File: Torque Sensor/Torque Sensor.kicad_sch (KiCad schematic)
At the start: 9 parts, among them U2 MCP3561R, U4 AP2112K-3.3 (REG LINEAR 3.3V)

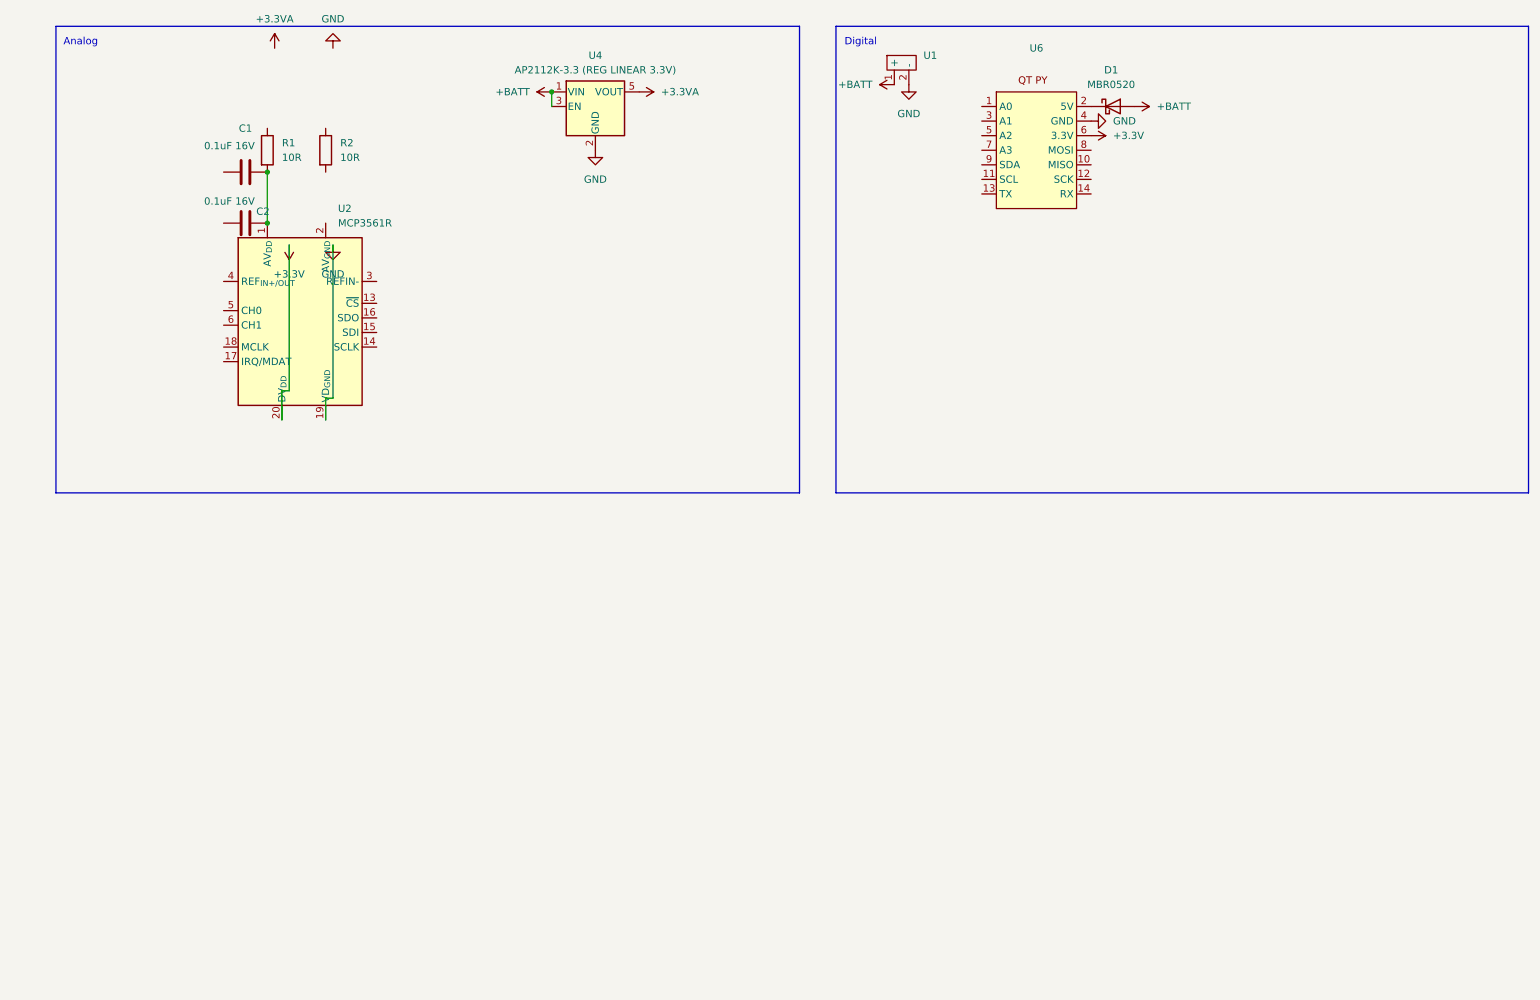
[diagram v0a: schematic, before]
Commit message: Reverted to older schematic
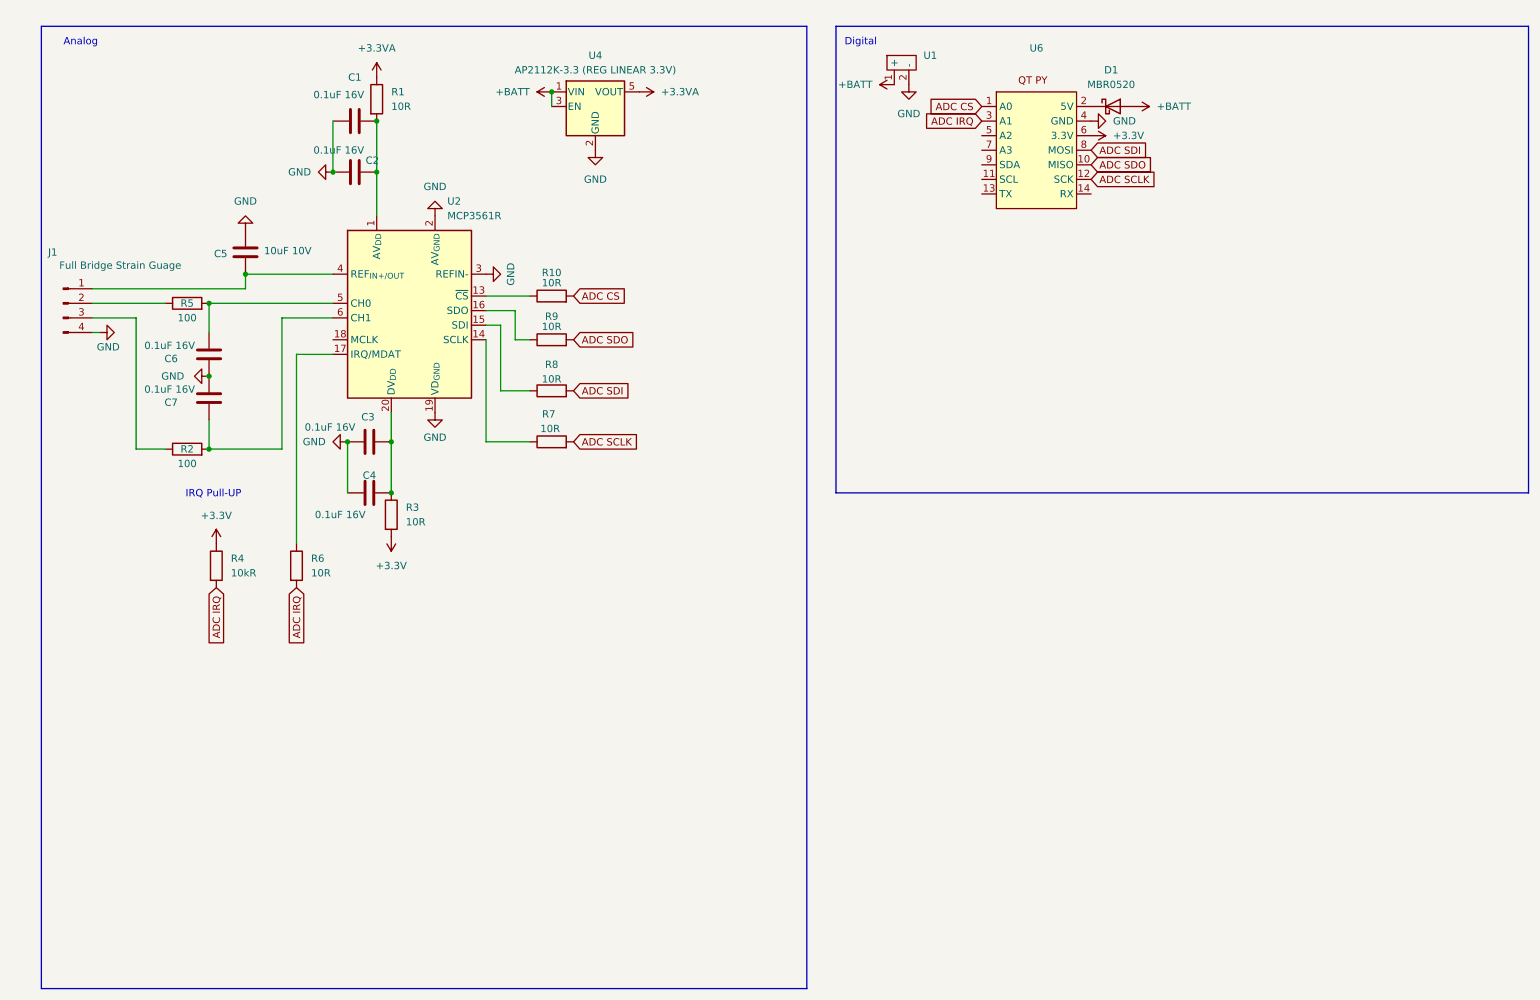
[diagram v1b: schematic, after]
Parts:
- added C3, C4, C6, C7: 0.1uF 16V, symbol Device:C
- added C5: 10uF 10V, symbol Device:C
- added J1: Full Bridge Strain Guage, symbol Connector:Conn_01x04_Pin
- added R10, R3, R6, R7, R8, R9: 10R, symbol Device:R
- added R4: 10kR, symbol Device:R
- added R5: 100, symbol Device:R
- R2: value 10R -> 100
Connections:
- net +3.3V: now also R3.2, R4.1; no longer U2.20 (DV_{DD})
- net +3.3VA: now also R1.1
- net GND: now also C1.1, C2.1, U2.2 (AV_{GND}), U2.3 (REFIN-), C3.1, C4.1, C5.2, C6.1, C7.2, J1.4 (Pin_4)
- net ADC CS: now reaches U6.1 (A0)
- net ADC CS: now also R10.2
- net ADC SDO: now reaches U6.10 (MISO)
- net ADC SDO: now also R9.2
- net ADC SCLK: now reaches U6.12 (SCK)
- net ADC SCLK: now also R7.2
- net ADC IRQ: now reaches U6.3 (A1)
- net ADC IRQ: now also R4.2, R6.2
- net ADC SDI: now reaches U6.8 (MOSI)
- net ADC SDI: now also R8.2
- net at U2.13 (~{CS}): now also R10.1
- net at U2.14 (SCLK): now also R7.1
- net at U2.15 (SDI): now also R8.1
- net at U2.16 (SDO): now also R9.1
- net at U2.17 (IRQ/MDAT): now also R6.1
- net at U2.4 (REF_{IN+/OUT}): now also C5.1, J1.1 (Pin_1)
- net at U2.5 (CH0): now also C6.2, R5.2
- net at U2.6 (CH1): now also R2.2, C7.1
- net at R2.1: now also J1.3 (Pin_3)
- new net: J1.2 (Pin_2), R5.1
- new net: C3.2, C4.2, R3.1, U2.20 (DV_{DD})
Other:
- note added: "IRQ Pull-UP"
- moved on the sheet: C1, C2, R1, U2

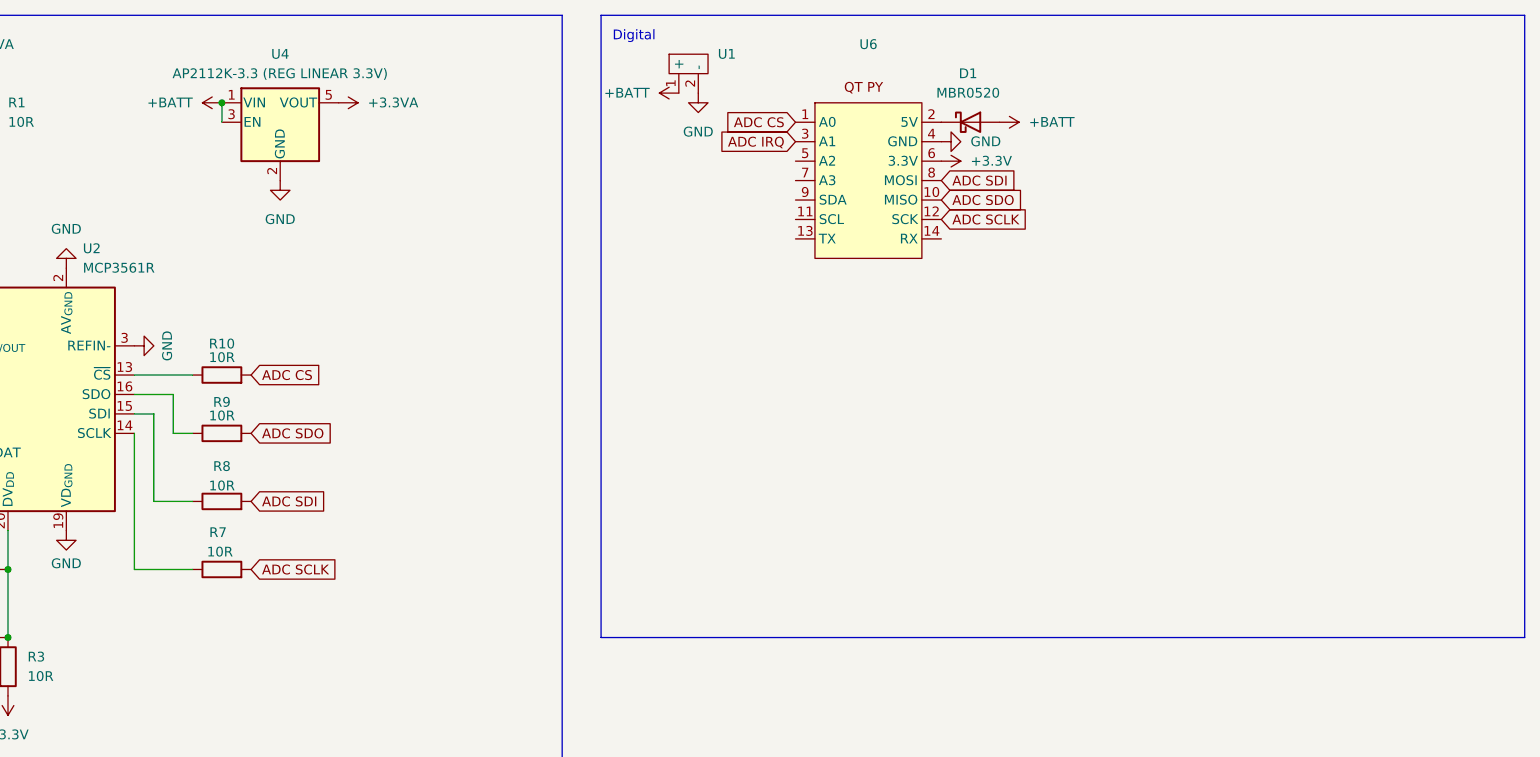
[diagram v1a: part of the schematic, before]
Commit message: Changed board to Feather rp2040 for charging circuitry, assigned footprints to caps and resistors.
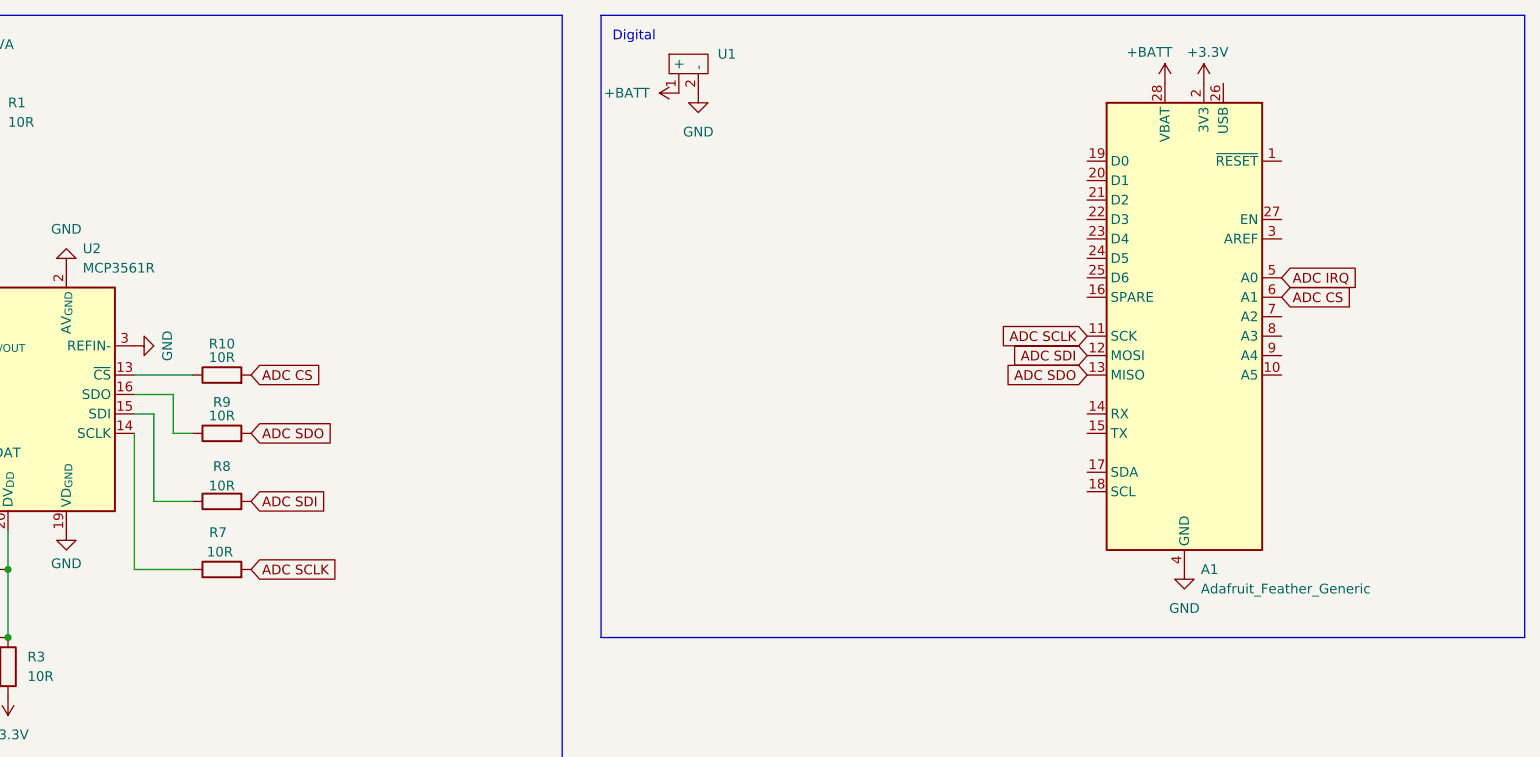
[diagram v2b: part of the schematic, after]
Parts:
- removed D1: MBR0520, Diode_SMD:D_SOD-123, symbol Diode:MBR0520
- removed U4: AP2112K-3.3 (REG LINEAR 3.3V), Package_TO_SOT_SMD:SOT-23-5, symbol Regulator_Linear:AP2112K-3.3
- removed U6: ~, TestLib:Adafruit QT PY, symbol New_Library:QT_PY
- added A1: Adafruit_Feather_Generic, Module:Adafruit_Feather, symbol MCU_Module:Adafruit_Feather_Generic
- C1, C2, C3, C4, C5, C6, C7: footprint (none) -> Capacitor_SMD:C_0805_2012Metric
- J1: footprint (none) -> Connector_PinHeader_1.00mm:PinHeader_1x04_P1.00mm_Vertical
- R1, R10, R2, R3, R4, R5, R6, R7, R8, R9: footprint (none) -> Resistor_SMD:R_0805_2012Metric
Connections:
- net +3.3V: now also A1.2 (3V3)
- net +BATT: now also A1.28 (VBAT)
- net ADC CS: now also A1.6 (A1)
- net ADC IRQ: now also A1.5 (A0)
- net ADC SCLK: now also A1.11 (SCK)
- net ADC SDI: now also A1.12 (MOSI)
- net ADC SDO: now also A1.13 (MISO)
- net GND: now also A1.4 (GND)

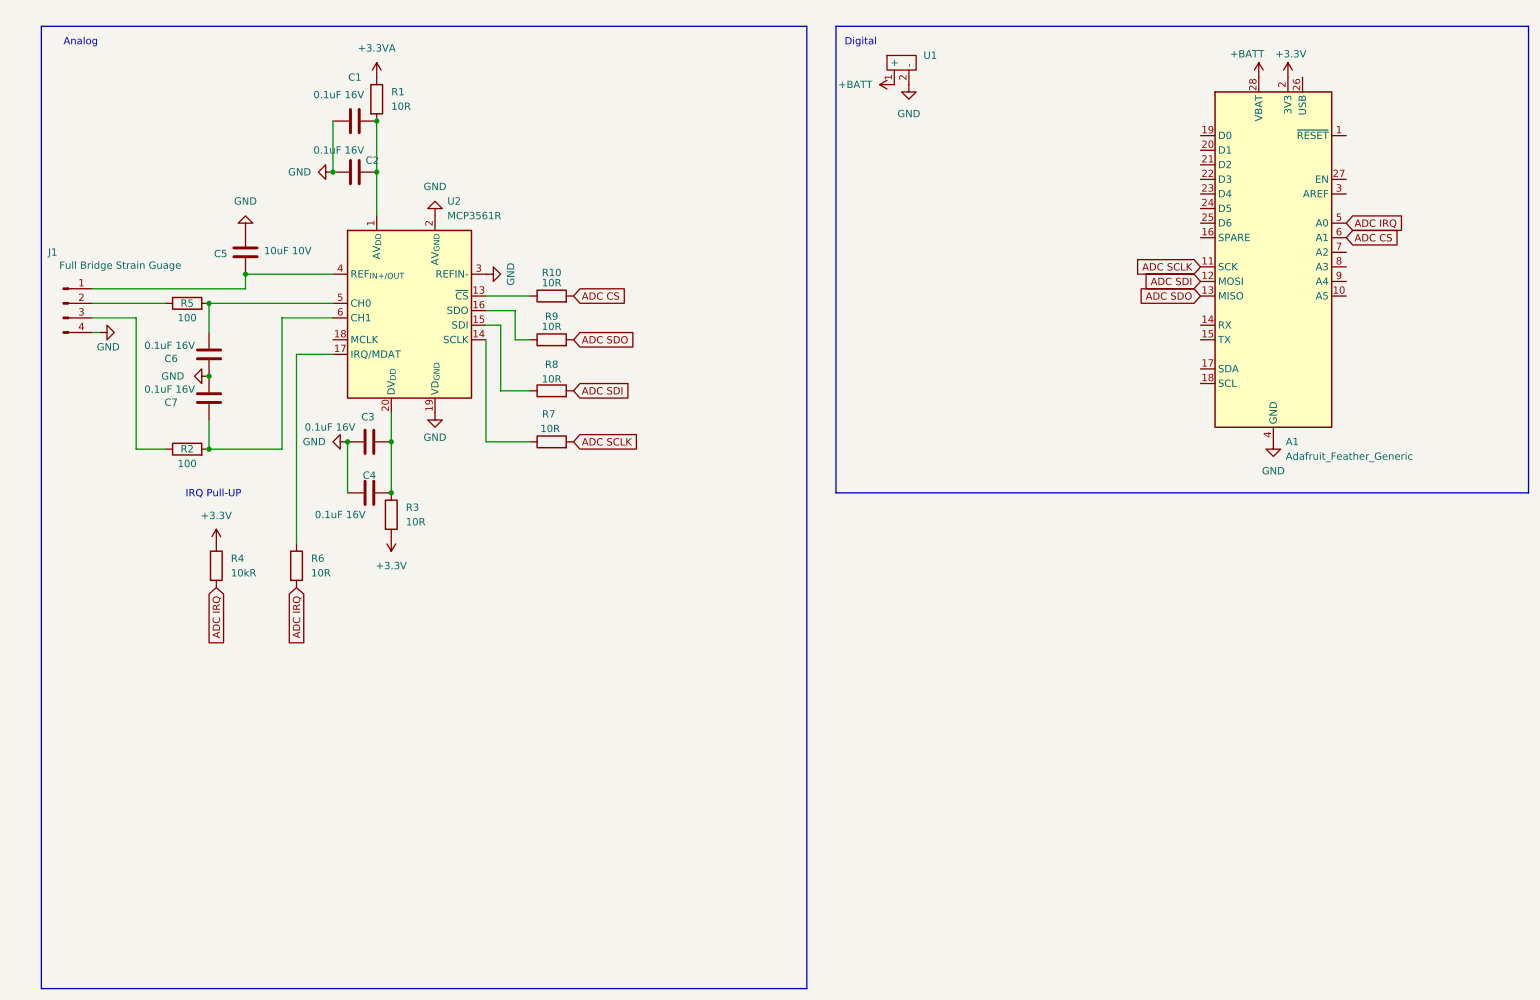
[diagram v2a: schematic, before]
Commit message: Changed ADC to the more JLC stocked AD7173-8 (Rev. B)
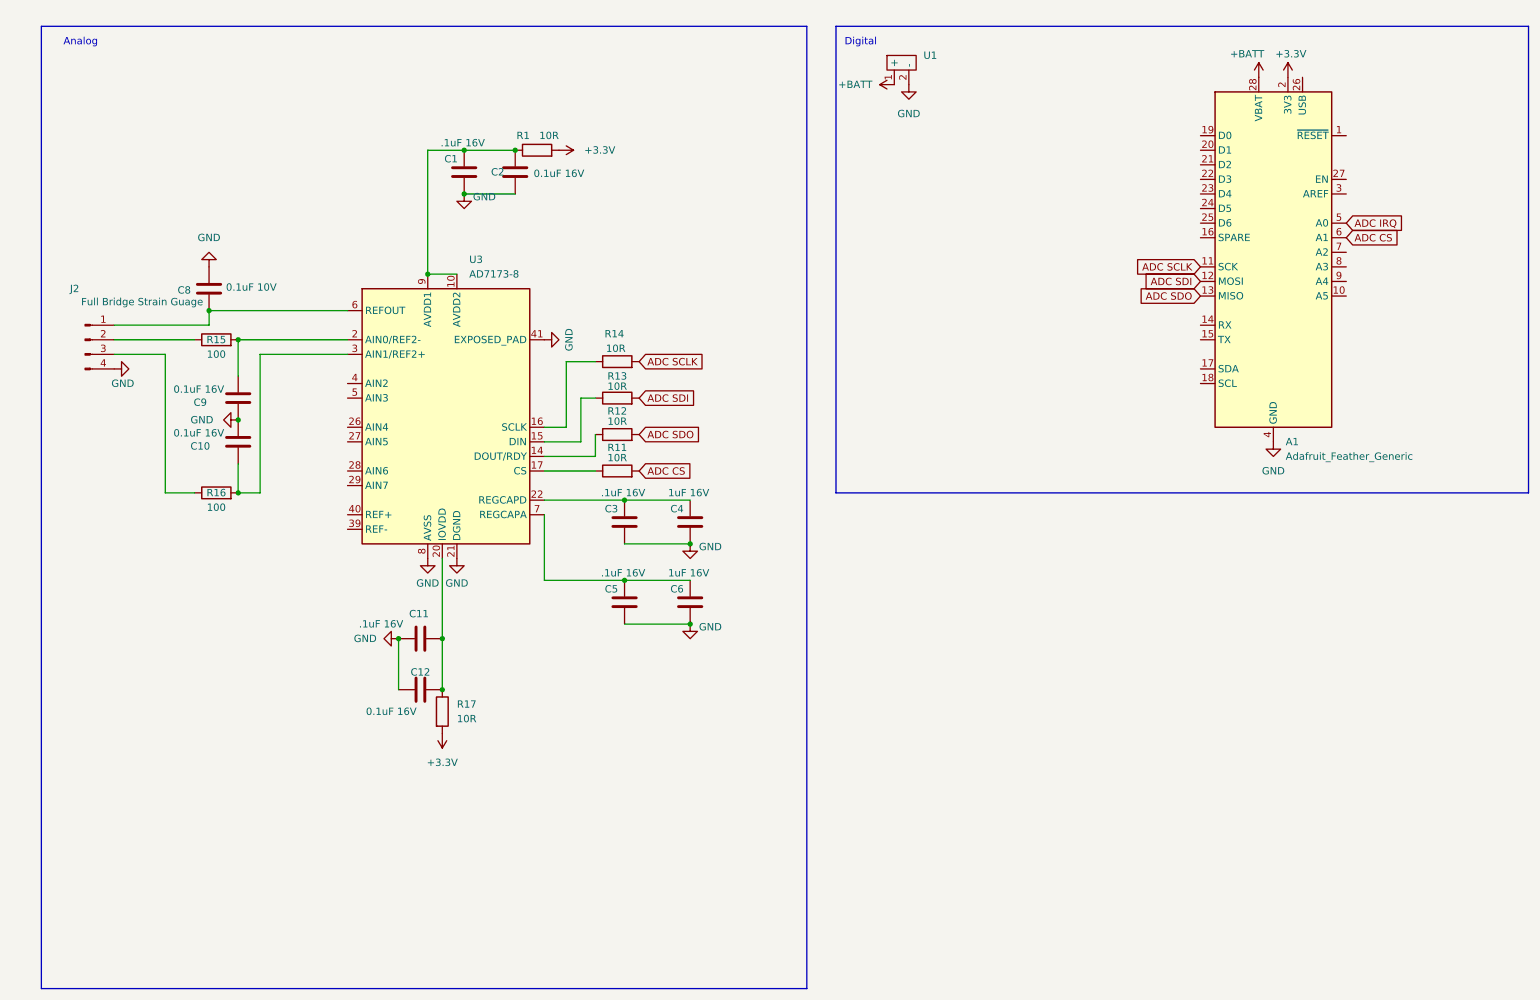
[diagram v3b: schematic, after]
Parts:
- removed C7: 0.1uF 16V, Capacitor_SMD:C_0805_2012Metric, symbol Device:C
- removed J1: Full Bridge Strain Guage, Connector_PinHeader_1.00mm:PinHeader_1x04_P1.00mm_Vertical, symbol Connector:Conn_01x04_Pin
- removed R10, R3, R6, R7, R8, R9: 10R, Resistor_SMD:R_0805_2012Metric, symbol Device:R
- removed R2, R5: 100, Resistor_SMD:R_0805_2012Metric, symbol Device:R
- removed R4: 10kR, Resistor_SMD:R_0805_2012Metric, symbol Device:R
- removed U2: MCP3561R, Package_SO:TSSOP-20_4.4x6.5mm_P0.65mm, symbol Analog_ADC:AD7327
- added C10, C12, C9: 0.1uF 16V, Capacitor_SMD:C_0805_2012Metric, symbol Device:C
- added C11: .1uF 16V, Capacitor_SMD:C_0805_2012Metric, symbol Device:C
- added C8: 0.1uF 10V, Capacitor_SMD:C_0805_2012Metric, symbol Device:C
- added J2: Full Bridge Strain Guage, Connector_PinHeader_1.00mm:PinHeader_1x04_P1.00mm_Vertical, symbol Connector:Conn_01x04_Pin
- added R11, R12, R13, R14, R17: 10R, Resistor_SMD:R_0805_2012Metric, symbol Device:R
- added R15, R16: 100, Resistor_SMD:R_0805_2012Metric, symbol Device:R
- added U3: AD7173-8, Package_CSP:LFCSP-40-1EP_6x6mm_P0.5mm_EP3.9x3.9mm, symbol New_Library:AD7173-8
- C1, C3: value 0.1uF 16V -> .1uF 16V
- C4, C6: value 0.1uF 16V -> 1uF 16V
- C5: value 10uF 10V -> .1uF 16V
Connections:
- net +3.3VA is gone; now on net AVDD: R1.1
- net +3.3V: now also R1.2, R17.2
- net ADC CS: now also R11.2
- net ADC SCLK: now also R14.2
- net ADC SDI: now also R13.2
- net ADC SDO: now also R12.2
- net GND: now also C5.1, C10.2, C11.1, C12.1, C8.2, C9.1, J2.4 (Pin_4), U3.21 (DGND), U3.22 (REGCAPD), U3.28 (AGND), U3.29 (AGND), U3.41 (EXPOSED_PAD), U3.5 (AGND), U3.8 (NC); no longer C5.2
- net AVDD: now reaches C1.2, C2.2
- net AVDD: now also U3.10 (AVDD2), U3.4 (AVDD), U3.40 (AVDD), U3.9 (AVDD1); no longer R1.2
- net at C3.2, C4.2: now also U3.22 (REGCAPD)
- net at C6.2: now also C5.2, U3.7 (REGCAPA)
- new net: C10.1, R16.2, U3.3 (AIN1/REF2+)
- new net: C9.2, R15.2, U3.2 (AIN0/REF2-)
- new net: C8.1, J2.1 (Pin_1), U3.6 (REFOUT)
- new net: J2.2 (Pin_2), R15.1
- new net: J2.3 (Pin_3), R16.1
- new net: R12.1, U3.14 (DOUT/RDY)
- new net: R14.1, U3.16 (SCLK)
- new net: C11.2, C12.2, R17.1, U3.20 (IOVDD)
- new net: R11.1, U3.17 (CS)
- new net: R13.1, U3.15 (DIN)
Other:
- note removed: "IRQ Pull-UP"
